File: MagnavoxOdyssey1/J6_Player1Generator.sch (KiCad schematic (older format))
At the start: 19 parts

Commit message: a lot more...
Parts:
- renumbered 7_C1 to 8_C1, 7_C2 to 8_C2, 7_C3 to 8_C3, 7_C4 to 8_C4, 7_C5 to 8_C5, 7_D1 to 8_D1, 7_D2 to 8_D2, 7_Q1 to 8_Q1, 7_Q2 to 8_Q2, 7_Q3 to 8_Q3, 7_Q4 to 8_Q4, 7_R1 to 8_R1, 7_R2 to 8_R2, 7_R3 to 8_R3, 7_R4 to 8_R4, 7_R5 to 8_R5, 7_R6 to 8_R6, 7_R7 to 8_R7, 7_R8 to 8_R8
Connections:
- net (8)_NC renamed (8)
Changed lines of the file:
@@
 (9)
 $Comp
-L DIODE 7_D1
+L DIODE 8_D1
 U 1 1 588DCAB3
 P 3500 3150
+AR Path="/58904212/588DCAB3" Ref="8_D1"  Part="1"
+AR Path="/588DC7EC/588DCAB3" Ref="7_D1"  Part="1"
+AR Path="/5891515D/588DCAB3" Ref="7_D1"  Part="1"
 F 0 "7_D1" H 3500 3342 40  0000 C CNN
 F 1 "DIODE" H 3500 3266 40  0000 C CNN
@@
 $EndComp
 $Comp
-L R 7_R1
+L R 8_R1
 U 1 1 588DCB1F
 P 3500 2500
+AR Path="/58904212/588DCB1F" Ref="8_R1"  Part="1"
+AR Path="/588DC7EC/588DCB1F" Ref="7_R1"  Part="1"
+AR Path="/5891515D/588DCB1F" Ref="7_R1"  Part="1"
 F 0 "7_R1" V 3315 2500 40  0000 C CNN
 F 1 "10k" V 3391 2500 40  0000 C CNN
@@
 $EndComp
 $Comp
-L CP1 7_C1
+L CP1 8_C1
 U 1 1 588DCB74
 P 4450 2500
+AR Path="/58904212/588DCB74" Ref="8_C1"  Part="1"
+AR Path="/588DC7EC/588DCB74" Ref="7_C1"  Part="1"
+AR Path="/5891515D/588DCB74" Ref="7_C1"  Part="1"
 F 0 "7_C1" V 4720 2500 50  0000 C CNN
 F 1 "1500" V 4629 2500 50  0000 C CNN
@@
 $EndComp
 $Comp
-L R 7_R2
+L R 8_R2
 U 1 1 588DCBFC
 P 4950 2900
+AR Path="/58904212/588DCBFC" Ref="8_R2"  Part="1"
+AR Path="/588DC7EC/588DCBFC" Ref="7_R2"  Part="1"
+AR Path="/5891515D/588DCBFC" Ref="7_R2"  Part="1"
 F 0 "7_R2" H 4879 2862 40  0000 R CNN
 F 1 "100k 5%" H 4879 2938 40  0000 R CNN
@@
 $EndComp
 $Comp
-L NPN 7_Q1
+L NPN 8_Q1
 U 1 1 588DCC63
 P 5500 2500
+AR Path="/58904212/588DCC63" Ref="8_Q1"  Part="1"
+AR Path="/588DC7EC/588DCC63" Ref="7_Q1"  Part="1"
+AR Path="/5891515D/588DCC63" Ref="7_Q1"  Part="1"
 F 0 "7_Q1" H 5691 2546 50  0000 L CNN
 F 1 "142N9" H 5691 2455 50  0000 L CNN
@@
 $EndComp
 $Comp
-L GND #PWR023
+L GND #PWR043
 U 1 1 588DCD18
 P 5600 2900
-F 0 "#PWR023" H 5600 2900 30  0001 C CNN
+AR Path="/58904212/588DCD18" Ref="#PWR043"  Part="1"
+AR Path="/588DC7EC/588DCD18" Ref="#PWR027"  Part="1"
+AR Path="/5891515D/588DCD18" Ref="#PWR043"  Part="1"
+F 0 "#PWR043" H 5600 2900 30  0001 C CNN
 F 1 "GND" H 5600 2830 30  0001 C CNN
 F 2 "" H 5600 2900 60  0001 C CNN
@@
 $EndComp
 $Comp
-L R 7_R3
+L R 8_R3
 U 1 1 588DCD72
 P 6300 2900
+AR Path="/58904212/588DCD72" Ref="8_R3"  Part="1"
+AR Path="/588DC7EC/588DCD72" Ref="7_R3"  Part="1"
+AR Path="/5891515D/588DCD72" Ref="7_R3"  Part="1"
 F 0 "7_R3" H 6229 2862 40  0000 R CNN
 F 1 "10k" H 6229 2938 40  0000 R CNN
@@
 $EndComp
 $Comp
-L CP1 7_C2
+L CP1 8_C2
 U 1 1 588DCDCD
 P 6800 2500
+AR Path="/58904212/588DCDCD" Ref="8_C2"  Part="1"
+AR Path="/588DC7EC/588DCDCD" Ref="7_C2"  Part="1"
+AR Path="/5891515D/588DCDCD" Ref="7_C2"  Part="1"
 F 0 "7_C2" V 7070 2500 50  0000 C CNN
 F 1 "120" V 6979 2500 50  0000 C CNN
@@
 $EndComp
 $Comp
-L NPN 7_Q2
+L NPN 8_Q2
 U 1 1 588DCE86
 P 7850 2500
+AR Path="/58904212/588DCE86" Ref="8_Q2"  Part="1"
+AR Path="/588DC7EC/588DCE86" Ref="7_Q2"  Part="1"
+AR Path="/5891515D/588DCE86" Ref="7_Q2"  Part="1"
 F 0 "7_Q2" H 8041 2546 50  0000 L CNN
 F 1 "142N9" H 8041 2455 50  0000 L CNN
@@
 $EndComp
 $Comp
-L GND #PWR024
+L GND #PWR044
 U 1 1 588DCE8C
 P 7950 2900
-F 0 "#PWR024" H 7950 2900 30  0001 C CNN
+AR Path="/58904212/588DCE8C" Ref="#PWR044"  Part="1"
+AR Path="/588DC7EC/588DCE8C" Ref="#PWR028"  Part="1"
+AR Path="/5891515D/588DCE8C" Ref="#PWR044"  Part="1"
+F 0 "#PWR044" H 7950 2900 30  0001 C CNN
 F 1 "GND" H 7950 2830 30  0001 C CNN
 F 2 "" H 7950 2900 60  0001 C CNN
@@
 $EndComp
 $Comp
-L R 7_R6
+L R 8_R6
 U 1 1 588DD03A
 P 4950 3950
+AR Path="/58904212/588DD03A" Ref="8_R6"  Part="1"
+AR Path="/588DC7EC/588DD03A" Ref="7_R6"  Part="1"
+AR Path="/5891515D/588DD03A" Ref="7_R6"  Part="1"
 F 0 "7_R6" H 4879 3912 40  0000 R CNN
 F 1 "270k 5%" H 4879 3988 40  0000 R CNN
@@
 $EndComp
 $Comp
-L NPN 7_Q3
+L NPN 8_Q3
 U 1 1 588DD5E2
 P 5500 4400
+AR Path="/58904212/588DD5E2" Ref="8_Q3"  Part="1"
+AR Path="/588DC7EC/588DD5E2" Ref="7_Q3"  Part="1"
+AR Path="/5891515D/588DD5E2" Ref="7_Q3"  Part="1"
 F 0 "7_Q3" H 5691 4446 50  0000 L CNN
 F 1 "142N10" H 5691 4355 50  0000 L CNN
@@
 $EndComp
 $Comp
-L GND #PWR025
+L GND #PWR045
 U 1 1 588DD5E8
 P 5600 4800
-F 0 "#PWR025" H 5600 4800 30  0001 C CNN
+AR Path="/58904212/588DD5E8" Ref="#PWR045"  Part="1"
+AR Path="/588DC7EC/588DD5E8" Ref="#PWR029"  Part="1"
+AR Path="/5891515D/588DD5E8" Ref="#PWR045"  Part="1"
+F 0 "#PWR045" H 5600 4800 30  0001 C CNN
 F 1 "GND" H 5600 4730 30  0001 C CNN
 F 2 "" H 5600 4800 60  0001 C CNN
@@
 	4950 4200 4950 4550
 $Comp
-L R 7_R7
+L R 8_R7
 U 1 1 588DD6AF
 P 6300 3700
+AR Path="/58904212/588DD6AF" Ref="8_R7"  Part="1"
+AR Path="/588DC7EC/588DD6AF" Ref="7_R7"  Part="1"
+AR Path="/5891515D/588DD6AF" Ref="7_R7"  Part="1"
 F 0 "7_R7" H 6229 3662 40  0000 R CNN
 F 1 "10k" H 6229 3738 40  0000 R CNN
@@
 	5600 4050 6300 4050
 $Comp
-L CP1 7_C4
+L CP1 8_C4
 U 1 1 588DD883
 P 6650 4200
+AR Path="/58904212/588DD883" Ref="8_C4"  Part="1"
+AR Path="/588DC7EC/588DD883" Ref="7_C4"  Part="1"
+AR Path="/5891515D/588DD883" Ref="7_C4"  Part="1"
 F 0 "7_C4" V 6920 4200 50  0000 C CNN
 F 1 "0.1" V 6829 4200 50  0000 C CNN
@@
 $EndComp
 $Comp
-L CP1 7_C5
+L CP1 8_C5
 U 1 1 588DD8E3
 P 7350 4700
+AR Path="/58904212/588DD8E3" Ref="8_C5"  Part="1"
+AR Path="/588DC7EC/588DD8E3" Ref="7_C5"  Part="1"
+AR Path="/5891515D/588DD8E3" Ref="7_C5"  Part="1"
 F 0 "7_C5" H 7483 4746 50  0000 L CNN
 F 1 "0.01" H 7483 4655 50  0000 L CNN
@@
 Connection ~ 6300 4050
 $Comp
-L CP1 7_C3
+L CP1 8_C3
 U 1 1 588DDB1C
 P 4950 4750
+AR Path="/58904212/588DDB1C" Ref="8_C3"  Part="1"
+AR Path="/588DC7EC/588DDB1C" Ref="7_C3"  Part="1"
+AR Path="/5891515D/588DDB1C" Ref="7_C3"  Part="1"
 F 0 "7_C3" H 5083 4796 50  0000 L CNN
 F 1 "45" H 5083 4705 50  0000 L CNN
@@
 (2)
 $Comp
-L R 7_R8
+L R 8_R8
 U 1 1 588DDD4B
 P 7900 5150
+AR Path="/58904212/588DDD4B" Ref="8_R8"  Part="1"
+AR Path="/588DC7EC/588DDD4B" Ref="7_R8"  Part="1"
+AR Path="/5891515D/588DDD4B" Ref="7_R8"  Part="1"
 F 0 "7_R8" V 8085 5150 40  0000 C CNN
 F 1 "10k" V 8009 5150 40  0000 C CNN
@@
 Connection ~ 7350 5150
 $Comp
-L NPN 7_Q4
+L NPN 8_Q4
 U 1 1 588DDF3A
 P 7850 4200
+AR Path="/58904212/588DDF3A" Ref="8_Q4"  Part="1"
+AR Path="/588DC7EC/588DDF3A" Ref="7_Q4"  Part="1"
+AR Path="/5891515D/588DDF3A" Ref="7_Q4"  Part="1"
 F 0 "7_Q4" H 8041 4246 50  0000 L CNN
 F 1 "142N9" H 8041 4155 50  0000 L CNN
@@
 $EndComp
 $Comp
-L GND #PWR026
+L GND #PWR046
 U 1 1 588DDF40
 P 7950 4600
-F 0 "#PWR026" H 7950 4600 30  0001 C CNN
+AR Path="/58904212/588DDF40" Ref="#PWR046"  Part="1"
+AR Path="/588DC7EC/588DDF40" Ref="#PWR030"  Part="1"
+AR Path="/5891515D/588DDF40" Ref="#PWR046"  Part="1"
+F 0 "#PWR046" H 7950 4600 30  0001 C CNN
 F 1 "GND" H 7950 4530 30  0001 C CNN
 F 2 "" H 7950 4600 60  0001 C CNN
@@
 Connection ~ 8500 3850
 $Comp
-L R 7_R4
+L R 8_R4
 U 1 1 588DE2ED
 P 7300 3300
+AR Path="/58904212/588DE2ED" Ref="8_R4"  Part="1"
+AR Path="/588DC7EC/588DE2ED" Ref="7_R4"  Part="1"
+AR Path="/5891515D/588DE2ED" Ref="7_R4"  Part="1"
 F 0 "7_R4" V 7485 3300 40  0000 C CNN
 F 1 "2.2k" V 7409 3300 40  0000 C CNN
@@
 $EndComp
 $Comp
-L R 7_R5
+L R 8_R5
 U 1 1 588DE379
 P 8100 3300
+AR Path="/58904212/588DE379" Ref="8_R5"  Part="1"
+AR Path="/588DC7EC/588DE379" Ref="7_R5"  Part="1"
+AR Path="/5891515D/588DE379" Ref="7_R5"  Part="1"
 F 0 "7_R5" V 8285 3300 40  0000 C CNN
 F 1 "10k" V 8209 3300 40  0000 C CNN
@@
 	7550 3300 7850 3300
 Text HLabel 8900 3600 2    60   Output ~ 0
-(8)_NC
+(8)
 Text HLabel 8950 2000 2    60   Output ~ 0
 (7)
@@
 Connection ~ 7250 2500
 $Comp
-L DIODE 7_D2
+L DIODE 8_D2
 U 1 1 588DE8DA
 P 3550 5150
+AR Path="/58904212/588DE8DA" Ref="8_D2"  Part="1"
+AR Path="/588DC7EC/588DE8DA" Ref="7_D2"  Part="1"
+AR Path="/5891515D/588DE8DA" Ref="7_D2"  Part="1"
 F 0 "7_D2" H 3550 5342 40  0000 C CNN
 F 1 "DIODE" H 3550 5266 40  0000 C CNN

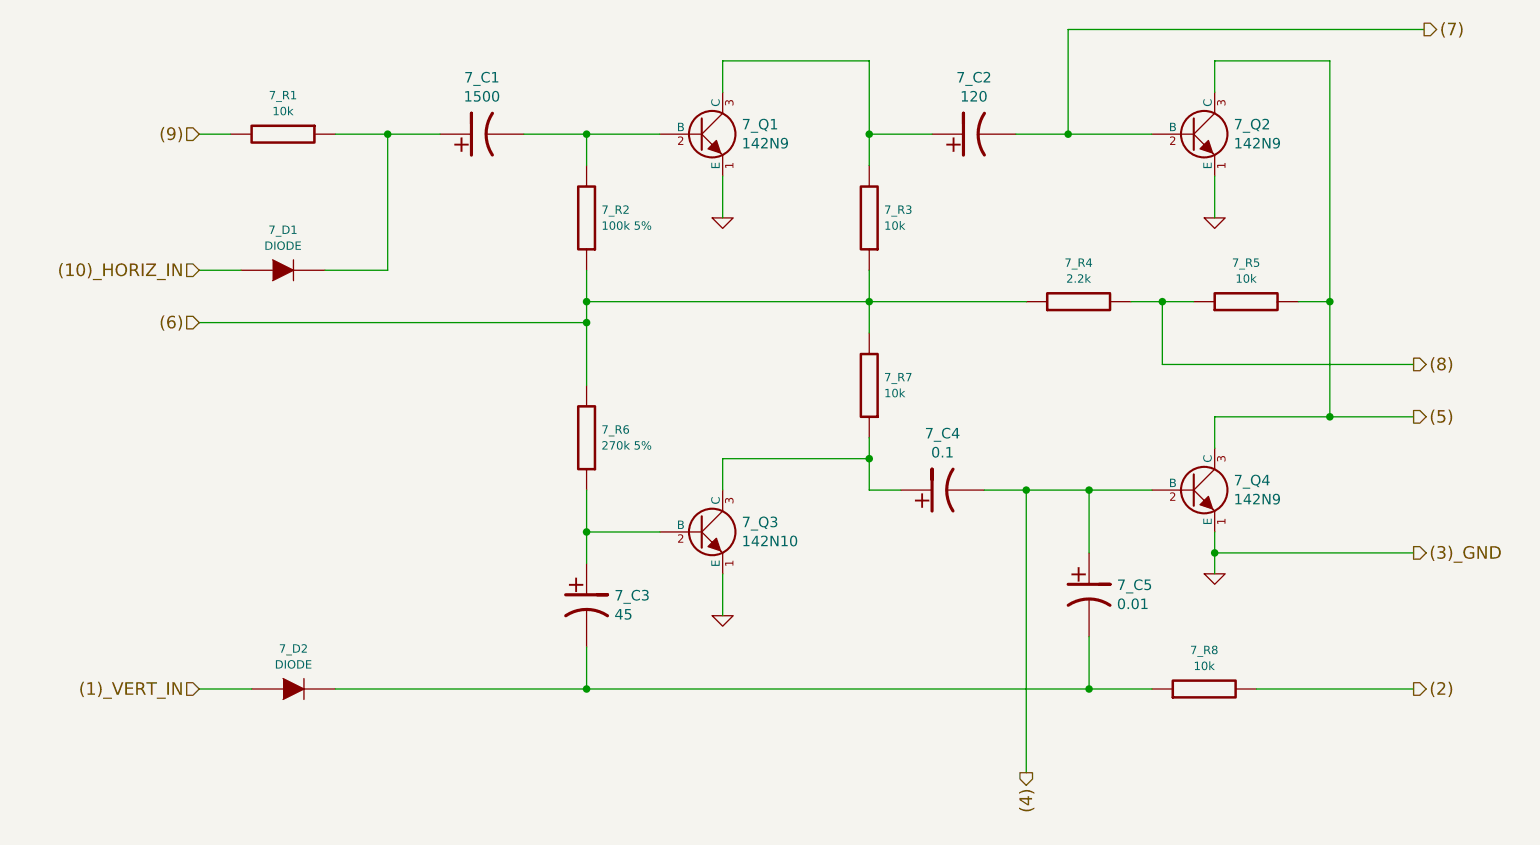
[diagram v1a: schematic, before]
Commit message: terminei de transcrever a PCB toda. Deixei de fora de propósito o estágio de modulação RF do sinal. É pouca coisa, posso adicionar amanhã ou depois... Gerei também um PDFão
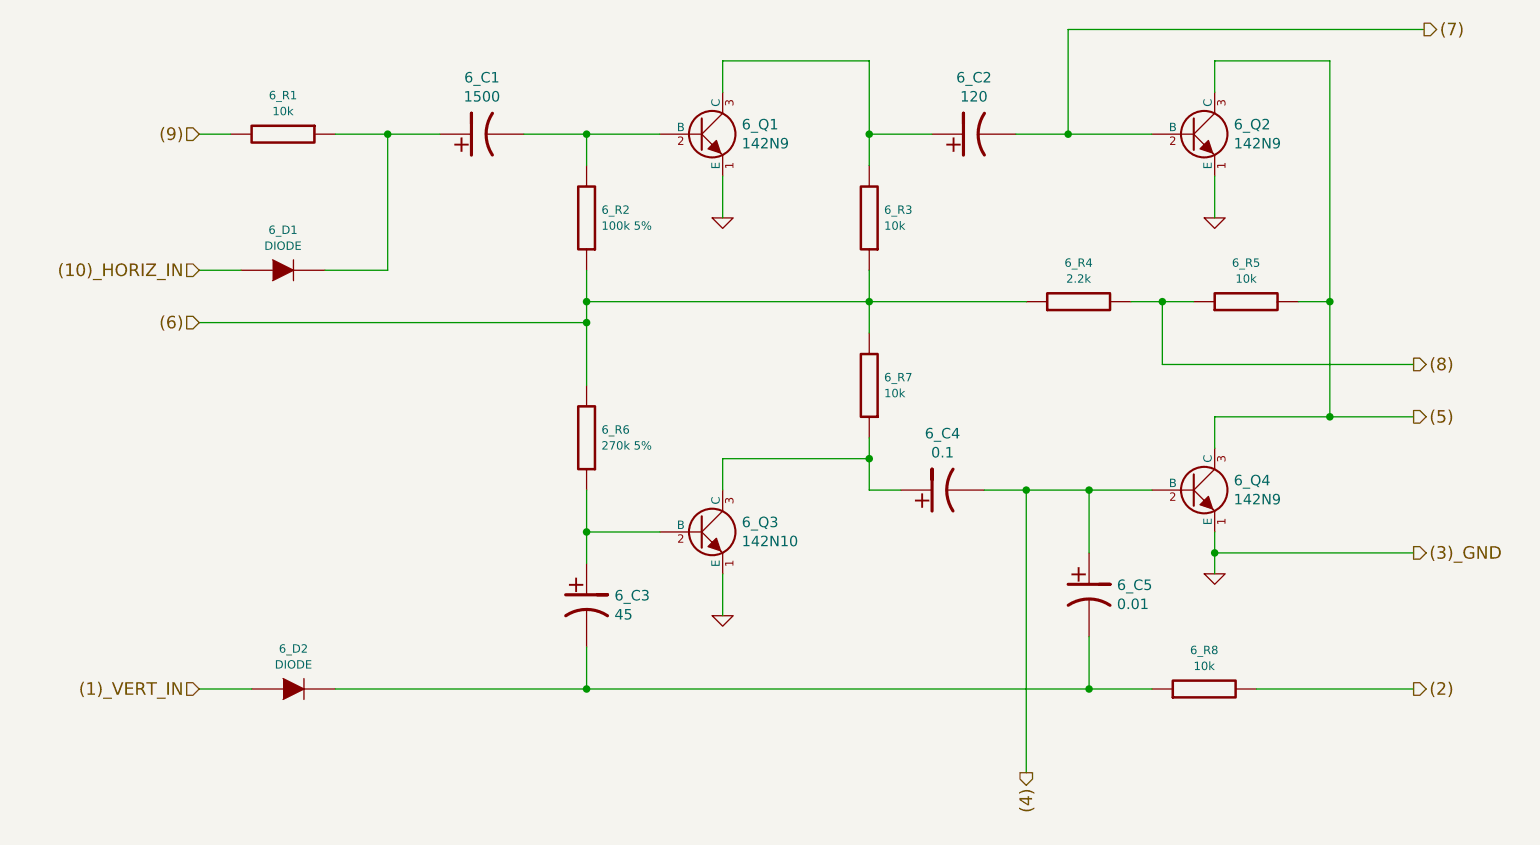
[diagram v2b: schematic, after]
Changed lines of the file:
@@
 $Descr A4 11693 8268
 encoding utf-8
-Sheet 4 9
+Sheet 9 12
 Title ""
 Date ""
@@
 AR Path="/58904212/588DCAB3" Ref="8_D1"  Part="1"
 AR Path="/588DC7EC/588DCAB3" Ref="7_D1"  Part="1"
-AR Path="/5891515D/588DCAB3" Ref="7_D1"  Part="1"
-F 0 "7_D1" H 3500 3342 40  0000 C CNN
+AR Path="/5891515D/588DCAB3" Ref="6_D1"  Part="1"
+F 0 "6_D1" H 3500 3342 40  0000 C CNN
 F 1 "DIODE" H 3500 3266 40  0000 C CNN
 F 2 "" H 3500 3150 60  0000 C CNN
@@
 AR Path="/58904212/588DCB1F" Ref="8_R1"  Part="1"
 AR Path="/588DC7EC/588DCB1F" Ref="7_R1"  Part="1"
-AR Path="/5891515D/588DCB1F" Ref="7_R1"  Part="1"
-F 0 "7_R1" V 3315 2500 40  0000 C CNN
+AR Path="/5891515D/588DCB1F" Ref="6_R1"  Part="1"
+F 0 "6_R1" V 3315 2500 40  0000 C CNN
 F 1 "10k" V 3391 2500 40  0000 C CNN
 F 2 "" V 3430 2500 30  0000 C CNN
@@
 AR Path="/58904212/588DCB74" Ref="8_C1"  Part="1"
 AR Path="/588DC7EC/588DCB74" Ref="7_C1"  Part="1"
-AR Path="/5891515D/588DCB74" Ref="7_C1"  Part="1"
-F 0 "7_C1" V 4720 2500 50  0000 C CNN
+AR Path="/5891515D/588DCB74" Ref="6_C1"  Part="1"
+F 0 "6_C1" V 4720 2500 50  0000 C CNN
 F 1 "1500" V 4629 2500 50  0000 C CNN
 F 2 "" H 4450 2500 60  0000 C CNN
@@
 AR Path="/58904212/588DCBFC" Ref="8_R2"  Part="1"
 AR Path="/588DC7EC/588DCBFC" Ref="7_R2"  Part="1"
-AR Path="/5891515D/588DCBFC" Ref="7_R2"  Part="1"
-F 0 "7_R2" H 4879 2862 40  0000 R CNN
+AR Path="/5891515D/588DCBFC" Ref="6_R2"  Part="1"
+F 0 "6_R2" H 4879 2862 40  0000 R CNN
 F 1 "100k 5%" H 4879 2938 40  0000 R CNN
 F 2 "" V 4880 2900 30  0000 C CNN
@@
 AR Path="/58904212/588DCC63" Ref="8_Q1"  Part="1"
 AR Path="/588DC7EC/588DCC63" Ref="7_Q1"  Part="1"
-AR Path="/5891515D/588DCC63" Ref="7_Q1"  Part="1"
-F 0 "7_Q1" H 5691 2546 50  0000 L CNN
+AR Path="/5891515D/588DCC63" Ref="6_Q1"  Part="1"
+F 0 "6_Q1" H 5691 2546 50  0000 L CNN
 F 1 "142N9" H 5691 2455 50  0000 L CNN
 F 2 "" H 5500 2500 60  0000 C CNN
@@
 AR Path="/58904212/588DCD18" Ref="#PWR043"  Part="1"
 AR Path="/588DC7EC/588DCD18" Ref="#PWR027"  Part="1"
-AR Path="/5891515D/588DCD18" Ref="#PWR043"  Part="1"
-F 0 "#PWR043" H 5600 2900 30  0001 C CNN
+AR Path="/5891515D/588DCD18" Ref="#PWR073"  Part="1"
+F 0 "#PWR073" H 5600 2900 30  0001 C CNN
 F 1 "GND" H 5600 2830 30  0001 C CNN
 F 2 "" H 5600 2900 60  0001 C CNN
@@
 AR Path="/58904212/588DCD72" Ref="8_R3"  Part="1"
 AR Path="/588DC7EC/588DCD72" Ref="7_R3"  Part="1"
-AR Path="/5891515D/588DCD72" Ref="7_R3"  Part="1"
-F 0 "7_R3" H 6229 2862 40  0000 R CNN
+AR Path="/5891515D/588DCD72" Ref="6_R3"  Part="1"
+F 0 "6_R3" H 6229 2862 40  0000 R CNN
 F 1 "10k" H 6229 2938 40  0000 R CNN
 F 2 "" V 6230 2900 30  0000 C CNN
@@
 AR Path="/58904212/588DCDCD" Ref="8_C2"  Part="1"
 AR Path="/588DC7EC/588DCDCD" Ref="7_C2"  Part="1"
-AR Path="/5891515D/588DCDCD" Ref="7_C2"  Part="1"
-F 0 "7_C2" V 7070 2500 50  0000 C CNN
+AR Path="/5891515D/588DCDCD" Ref="6_C2"  Part="1"
+F 0 "6_C2" V 7070 2500 50  0000 C CNN
 F 1 "120" V 6979 2500 50  0000 C CNN
 F 2 "" H 6800 2500 60  0000 C CNN
@@
 AR Path="/58904212/588DCE86" Ref="8_Q2"  Part="1"
 AR Path="/588DC7EC/588DCE86" Ref="7_Q2"  Part="1"
-AR Path="/5891515D/588DCE86" Ref="7_Q2"  Part="1"
-F 0 "7_Q2" H 8041 2546 50  0000 L CNN
+AR Path="/5891515D/588DCE86" Ref="6_Q2"  Part="1"
+F 0 "6_Q2" H 8041 2546 50  0000 L CNN
 F 1 "142N9" H 8041 2455 50  0000 L CNN
 F 2 "" H 7850 2500 60  0000 C CNN
@@
 AR Path="/58904212/588DCE8C" Ref="#PWR044"  Part="1"
 AR Path="/588DC7EC/588DCE8C" Ref="#PWR028"  Part="1"
-AR Path="/5891515D/588DCE8C" Ref="#PWR044"  Part="1"
-F 0 "#PWR044" H 7950 2900 30  0001 C CNN
+AR Path="/5891515D/588DCE8C" Ref="#PWR074"  Part="1"
+F 0 "#PWR074" H 7950 2900 30  0001 C CNN
 F 1 "GND" H 7950 2830 30  0001 C CNN
 F 2 "" H 7950 2900 60  0001 C CNN
@@
 AR Path="/58904212/588DD03A" Ref="8_R6"  Part="1"
 AR Path="/588DC7EC/588DD03A" Ref="7_R6"  Part="1"
-AR Path="/5891515D/588DD03A" Ref="7_R6"  Part="1"
-F 0 "7_R6" H 4879 3912 40  0000 R CNN
+AR Path="/5891515D/588DD03A" Ref="6_R6"  Part="1"
+F 0 "6_R6" H 4879 3912 40  0000 R CNN
 F 1 "270k 5%" H 4879 3988 40  0000 R CNN
 F 2 "" V 4880 3950 30  0000 C CNN
@@
 AR Path="/58904212/588DD5E2" Ref="8_Q3"  Part="1"
 AR Path="/588DC7EC/588DD5E2" Ref="7_Q3"  Part="1"
-AR Path="/5891515D/588DD5E2" Ref="7_Q3"  Part="1"
-F 0 "7_Q3" H 5691 4446 50  0000 L CNN
+AR Path="/5891515D/588DD5E2" Ref="6_Q3"  Part="1"
+F 0 "6_Q3" H 5691 4446 50  0000 L CNN
 F 1 "142N10" H 5691 4355 50  0000 L CNN
 F 2 "" H 5500 4400 60  0000 C CNN
@@
 AR Path="/58904212/588DD5E8" Ref="#PWR045"  Part="1"
 AR Path="/588DC7EC/588DD5E8" Ref="#PWR029"  Part="1"
-AR Path="/5891515D/588DD5E8" Ref="#PWR045"  Part="1"
-F 0 "#PWR045" H 5600 4800 30  0001 C CNN
+AR Path="/5891515D/588DD5E8" Ref="#PWR075"  Part="1"
+F 0 "#PWR075" H 5600 4800 30  0001 C CNN
 F 1 "GND" H 5600 4730 30  0001 C CNN
 F 2 "" H 5600 4800 60  0001 C CNN
@@
 AR Path="/58904212/588DD6AF" Ref="8_R7"  Part="1"
 AR Path="/588DC7EC/588DD6AF" Ref="7_R7"  Part="1"
-AR Path="/5891515D/588DD6AF" Ref="7_R7"  Part="1"
-F 0 "7_R7" H 6229 3662 40  0000 R CNN
+AR Path="/5891515D/588DD6AF" Ref="6_R7"  Part="1"
+F 0 "6_R7" H 6229 3662 40  0000 R CNN
 F 1 "10k" H 6229 3738 40  0000 R CNN
 F 2 "" V 6230 3700 30  0000 C CNN
@@
 AR Path="/58904212/588DD883" Ref="8_C4"  Part="1"
 AR Path="/588DC7EC/588DD883" Ref="7_C4"  Part="1"
-AR Path="/5891515D/588DD883" Ref="7_C4"  Part="1"
-F 0 "7_C4" V 6920 4200 50  0000 C CNN
+AR Path="/5891515D/588DD883" Ref="6_C4"  Part="1"
+F 0 "6_C4" V 6920 4200 50  0000 C CNN
 F 1 "0.1" V 6829 4200 50  0000 C CNN
 F 2 "" H 6650 4200 60  0000 C CNN
@@
 AR Path="/58904212/588DD8E3" Ref="8_C5"  Part="1"
 AR Path="/588DC7EC/588DD8E3" Ref="7_C5"  Part="1"
-AR Path="/5891515D/588DD8E3" Ref="7_C5"  Part="1"
-F 0 "7_C5" H 7483 4746 50  0000 L CNN
+AR Path="/5891515D/588DD8E3" Ref="6_C5"  Part="1"
+F 0 "6_C5" H 7483 4746 50  0000 L CNN
 F 1 "0.01" H 7483 4655 50  0000 L CNN
 F 2 "" H 7350 4700 60  0000 C CNN
@@
 AR Path="/58904212/588DDB1C" Ref="8_C3"  Part="1"
 AR Path="/588DC7EC/588DDB1C" Ref="7_C3"  Part="1"
-AR Path="/5891515D/588DDB1C" Ref="7_C3"  Part="1"
-F 0 "7_C3" H 5083 4796 50  0000 L CNN
+AR Path="/5891515D/588DDB1C" Ref="6_C3"  Part="1"
+F 0 "6_C3" H 5083 4796 50  0000 L CNN
 F 1 "45" H 5083 4705 50  0000 L CNN
 F 2 "" H 4950 4750 60  0000 C CNN
@@
 AR Path="/58904212/588DDD4B" Ref="8_R8"  Part="1"
 AR Path="/588DC7EC/588DDD4B" Ref="7_R8"  Part="1"
-AR Path="/5891515D/588DDD4B" Ref="7_R8"  Part="1"
-F 0 "7_R8" V 8085 5150 40  0000 C CNN
+AR Path="/5891515D/588DDD4B" Ref="6_R8"  Part="1"
+F 0 "6_R8" V 8085 5150 40  0000 C CNN
 F 1 "10k" V 8009 5150 40  0000 C CNN
 F 2 "" V 7830 5150 30  0000 C CNN
@@
 AR Path="/58904212/588DDF3A" Ref="8_Q4"  Part="1"
 AR Path="/588DC7EC/588DDF3A" Ref="7_Q4"  Part="1"
-AR Path="/5891515D/588DDF3A" Ref="7_Q4"  Part="1"
-F 0 "7_Q4" H 8041 4246 50  0000 L CNN
+AR Path="/5891515D/588DDF3A" Ref="6_Q4"  Part="1"
+F 0 "6_Q4" H 8041 4246 50  0000 L CNN
 F 1 "142N9" H 8041 4155 50  0000 L CNN
 F 2 "" H 7850 4200 60  0000 C CNN
@@
 AR Path="/58904212/588DDF40" Ref="#PWR046"  Part="1"
 AR Path="/588DC7EC/588DDF40" Ref="#PWR030"  Part="1"
-AR Path="/5891515D/588DDF40" Ref="#PWR046"  Part="1"
-F 0 "#PWR046" H 7950 4600 30  0001 C CNN
+AR Path="/5891515D/588DDF40" Ref="#PWR076"  Part="1"
+F 0 "#PWR076" H 7950 4600 30  0001 C CNN
 F 1 "GND" H 7950 4530 30  0001 C CNN
 F 2 "" H 7950 4600 60  0001 C CNN
@@
 AR Path="/58904212/588DE2ED" Ref="8_R4"  Part="1"
 AR Path="/588DC7EC/588DE2ED" Ref="7_R4"  Part="1"
-AR Path="/5891515D/588DE2ED" Ref="7_R4"  Part="1"
-F 0 "7_R4" V 7485 3300 40  0000 C CNN
+AR Path="/5891515D/588DE2ED" Ref="6_R4"  Part="1"
+F 0 "6_R4" V 7485 3300 40  0000 C CNN
 F 1 "2.2k" V 7409 3300 40  0000 C CNN
 F 2 "" V 7230 3300 30  0000 C CNN
@@
 AR Path="/58904212/588DE379" Ref="8_R5"  Part="1"
 AR Path="/588DC7EC/588DE379" Ref="7_R5"  Part="1"
-AR Path="/5891515D/588DE379" Ref="7_R5"  Part="1"
-F 0 "7_R5" V 8285 3300 40  0000 C CNN
+AR Path="/5891515D/588DE379" Ref="6_R5"  Part="1"
+F 0 "6_R5" V 8285 3300 40  0000 C CNN
 F 1 "10k" V 8209 3300 40  0000 C CNN
 F 2 "" V 8030 3300 30  0000 C CNN
@@
 AR Path="/58904212/588DE8DA" Ref="8_D2"  Part="1"
 AR Path="/588DC7EC/588DE8DA" Ref="7_D2"  Part="1"
-AR Path="/5891515D/588DE8DA" Ref="7_D2"  Part="1"
-F 0 "7_D2" H 3550 5342 40  0000 C CNN
+AR Path="/5891515D/588DE8DA" Ref="6_D2"  Part="1"
+F 0 "6_D2" H 3550 5342 40  0000 C CNN
 F 1 "DIODE" H 3550 5266 40  0000 C CNN
 F 2 "" H 3550 5150 60  0000 C CNN
